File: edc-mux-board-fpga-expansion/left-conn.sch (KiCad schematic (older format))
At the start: 68 parts, among them J2 Device 8, J3 Device 9, J4 Device 10, J5 Device 11

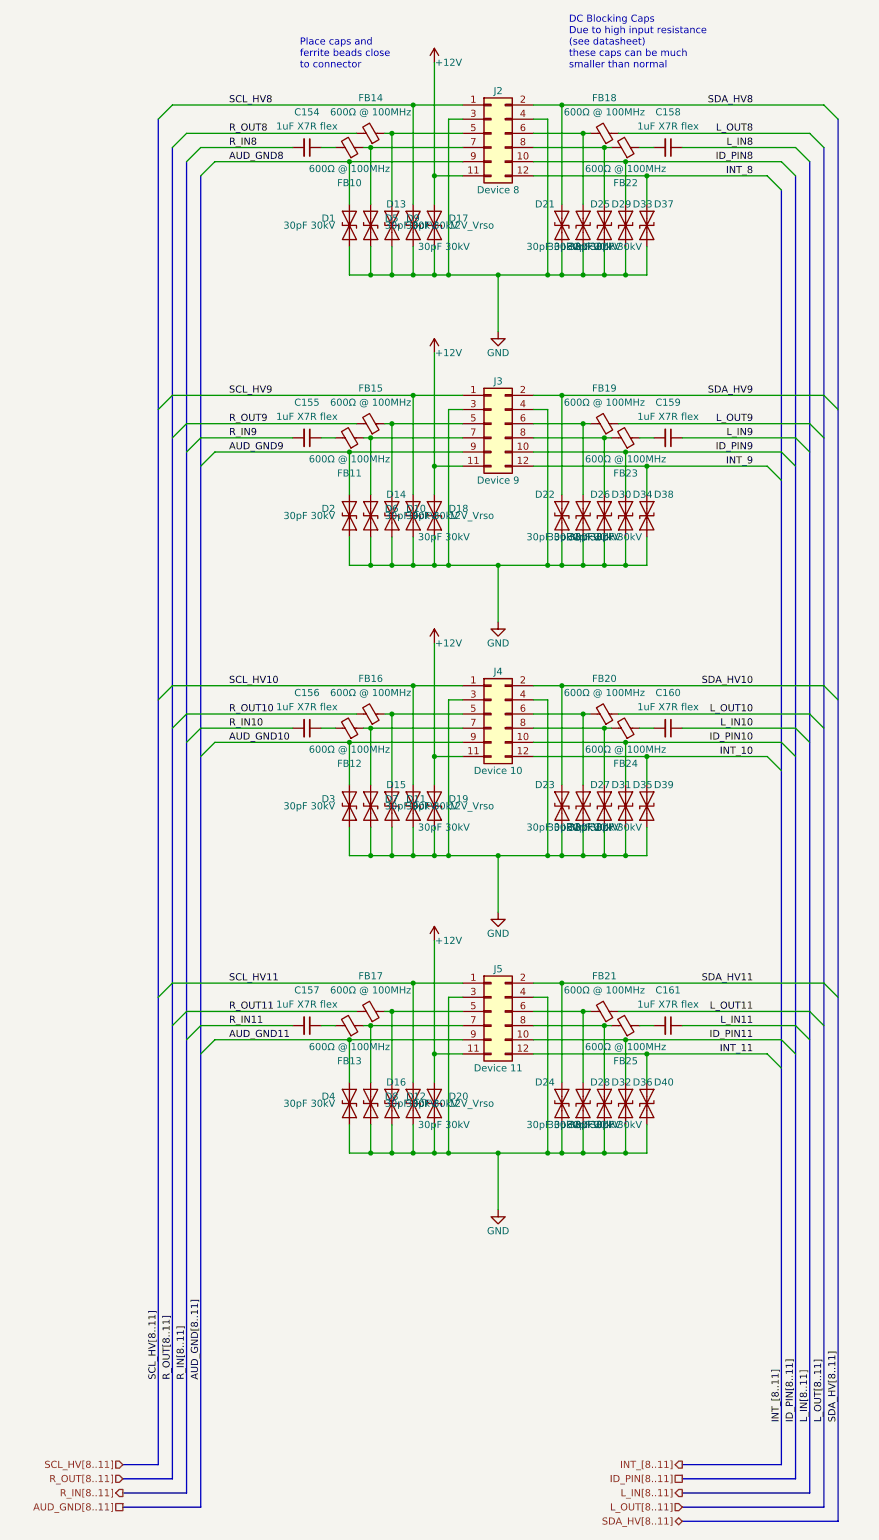
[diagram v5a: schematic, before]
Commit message: Reworking connector pinouts to simplify board layout of CODECs
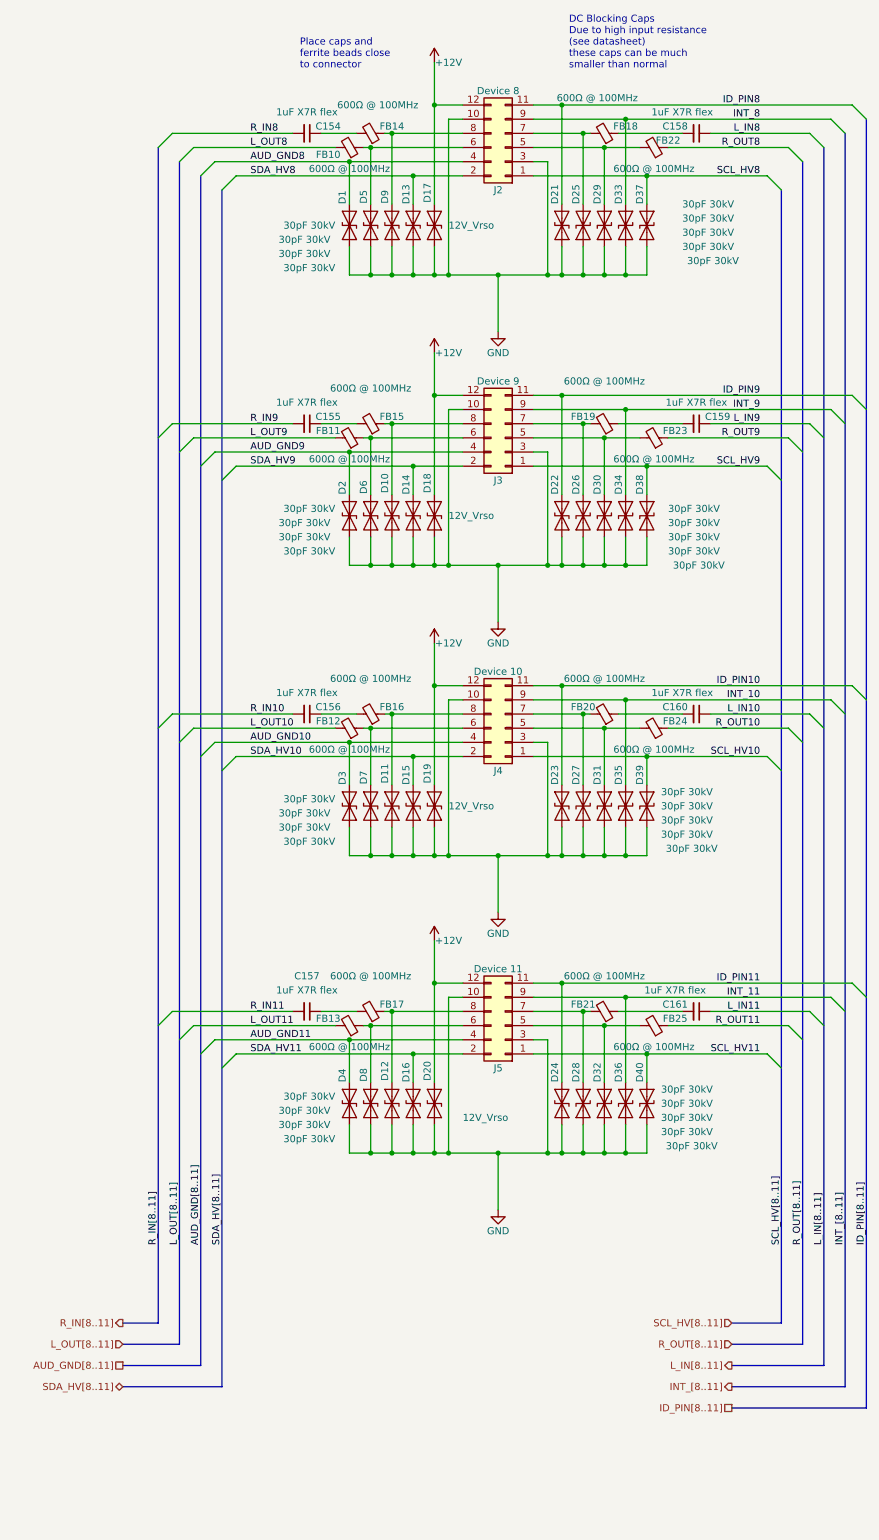
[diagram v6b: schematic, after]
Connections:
- net +12V: now also J2.12 (Pin_12), J3.12 (Pin_12), J4.12 (Pin_12), J5.12 (Pin_12); no longer J2.11 (Pin_11), J3.11 (Pin_11), J4.11 (Pin_11), J5.11 (Pin_11)
- net AUD_GND10: now also J4.4 (Pin_4); no longer J4.9 (Pin_9)
- net AUD_GND11: now also J5.4 (Pin_4); no longer J5.9 (Pin_9)
- net AUD_GND8: now also J2.4 (Pin_4); no longer J2.9 (Pin_9)
- net AUD_GND9: now also J3.4 (Pin_4); no longer J3.9 (Pin_9)
- net GND: now also J2.10 (Pin_10), J3.10 (Pin_10), J4.10 (Pin_10), J5.10 (Pin_10); no longer J2.4 (Pin_4), J3.4 (Pin_4), J4.4 (Pin_4), J5.4 (Pin_4)
- net ID_PIN10: now also D23.1 (A1), J4.11 (Pin_11); no longer D35.1 (A1), J4.10 (Pin_10)
- net ID_PIN11: now also D24.1 (A1), J5.11 (Pin_11); no longer D36.1 (A1), J5.10 (Pin_10)
- net ID_PIN8: now also D21.1 (A1), J2.11 (Pin_11); no longer D33.1 (A1), J2.10 (Pin_10)
- net ID_PIN9: now also D22.1 (A1), J3.11 (Pin_11); no longer D34.1 (A1), J3.10 (Pin_10)
- net INT_10: now also D35.1 (A1), J4.9 (Pin_9); no longer D39.1 (A1), J4.12 (Pin_12)
- net INT_11: now also D36.1 (A1), J5.9 (Pin_9); no longer D40.1 (A1), J5.12 (Pin_12)
- net INT_8: now also D33.1 (A1), J2.9 (Pin_9); no longer D37.1 (A1), J2.12 (Pin_12)
- net INT_9: now also D34.1 (A1), J3.9 (Pin_9); no longer D38.1 (A1), J3.12 (Pin_12)
- net L_OUT10: now also FB12.2; no longer FB20.1
- net L_OUT11: now also FB13.2; no longer FB21.1
- net L_OUT8: now also FB10.2; no longer FB18.1
- net L_OUT9: now also FB11.2; no longer FB19.1
- net R_OUT10: now also FB24.1; no longer FB16.2
- net R_OUT11: now also FB25.1; no longer FB17.2
- net R_OUT8: now also FB22.1; no longer FB14.2
- net R_OUT9: now also FB23.1; no longer FB15.2
- net SCL_HV10: now also D39.1 (A1); no longer D15.1 (A1)
- net SCL_HV11: now also D40.1 (A1); no longer D16.1 (A1)
- net SCL_HV8: now also D37.1 (A1); no longer D13.1 (A1)
- net SCL_HV9: now also D38.1 (A1); no longer D14.1 (A1)
- net SDA_HV10: now also D15.1 (A1); no longer D23.1 (A1)
- net SDA_HV11: now also D16.1 (A1); no longer D24.1 (A1)
- net SDA_HV8: now also D13.1 (A1); no longer D21.1 (A1)
- net SDA_HV9: now also D14.1 (A1); no longer D22.1 (A1)
- net at D9.1 (A1), FB14.1: now also J2.8 (Pin_8); no longer J2.5 (Pin_5)
- net at D25.1 (A1), FB18.2: now also J2.7 (Pin_7); no longer J2.6 (Pin_6)
- net at D5.1 (A1), FB10.1: now also J2.6 (Pin_6); no longer J2.7 (Pin_7)
- net at D29.1 (A1), FB22.2: now also J2.5 (Pin_5); no longer J2.8 (Pin_8)
- net at C154.1: now also FB14.2; no longer FB10.2
- net at C158.2: now also FB18.1; no longer FB22.1
- net at D10.1 (A1), FB15.1: now also J3.8 (Pin_8); no longer J3.5 (Pin_5)
- net at D26.1 (A1), FB19.2: now also J3.7 (Pin_7); no longer J3.6 (Pin_6)
- net at D6.1 (A1), FB11.1: now also J3.6 (Pin_6); no longer J3.7 (Pin_7)
- net at D30.1 (A1), FB23.2: now also J3.5 (Pin_5); no longer J3.8 (Pin_8)
- net at C155.1: now also FB15.2; no longer FB11.2
- net at C159.2: now also FB19.1; no longer FB23.1
- net at D11.1 (A1), FB16.1: now also J4.8 (Pin_8); no longer J4.5 (Pin_5)
- net at D27.1 (A1), FB20.2: now also J4.7 (Pin_7); no longer J4.6 (Pin_6)
- net at D7.1 (A1), FB12.1: now also J4.6 (Pin_6); no longer J4.7 (Pin_7)
- net at D31.1 (A1), FB24.2: now also J4.5 (Pin_5); no longer J4.8 (Pin_8)
- net at C156.1: now also FB16.2; no longer FB12.2
- net at C160.2: now also FB20.1; no longer FB24.1
- net at D12.1 (A1), FB17.1: now also J5.8 (Pin_8); no longer J5.5 (Pin_5)
- net at D28.1 (A1), FB21.2: now also J5.7 (Pin_7); no longer J5.6 (Pin_6)
- net at D8.1 (A1), FB13.1: now also J5.6 (Pin_6); no longer J5.7 (Pin_7)
- net at D32.1 (A1), FB25.2: now also J5.5 (Pin_5); no longer J5.8 (Pin_8)
- net at C157.1: now also FB17.2; no longer FB13.2
- net at C161.2: now also FB21.1; no longer FB25.1
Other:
- moved on the sheet: C154, C155, C156, C157, C158, C159, C160, C161, FB22, FB23, FB24, FB25

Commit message: removing extraneous AR Paths and organization
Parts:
- renumbered C160 to C166

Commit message: s/Manufacturers Part Number/MPN/g
for compatability with MacroFab automated processing
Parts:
- C154, C155, C156, C157, C158, C159, C161, C166: MPN (none) -> C0805X105J3RECAUTO; Manufacturers Part Number C0805X105J3RECAUTO -> (none)
- D1, D10, D11, D12, D13, D14, D15, D16, D2, D21, D22, D23, D24, D25, D26, D27, D28, D29, D3, D30, D31, D32, D33, D34, D35, D36, D37, D38, D39, D4, D40, D5, D6, D7, D8, D9: MPN (none) -> SP1005-01ETG; Manufacturers Part Number SP1005-01ETG -> (none)
- D17, D18, D19, D20: MPN (none) -> SMAJ12CA; Manufacturers Part Number SMAJ12CA -> (none)
- FB10, FB11, FB12, FB13, FB14, FB15, FB16, FB17, FB18, FB19, FB20, FB21, FB22, FB23, FB24, FB25: MPN (none) -> BLM21AG601SZ1D; Manufacturers Part Number BLM21AG601SZ1D -> (none)
- J2, J3, J4, J5: MPN (none) -> B12B-PHDSS(LF)(SN); Manufacturers Part Number B12B-PHDSS(LF)(SN) -> (none)
